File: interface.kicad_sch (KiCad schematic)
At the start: 58 parts

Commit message: More changes from review
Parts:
- removed C? (x3): C_100n_0402, antmicro-footprints:0402-cap, symbol antmicroCapacitors0402:C_100n_0402
- removed R? (x10): R_2k_0402, antmicro-footprints:0402-res, symbol antmicroResistors0402:R_2k_0402
- removed R? (x12): R_0R_0402, antmicro-footprints:0402-res, symbol antmicroResistors0402:R_0R_0402
- removed R? (x2): R_2k2_0402, antmicro-footprints:0402-res, symbol antmicroResistors0402:R_2k2_0402
- removed R?: R_10k_0402, antmicro-footprints:0402-res, symbol antmicroResistors0402:R_10k_0402
- removed SP? (x4): 9774110360, antmicro-footprints:Mounting_Wuerth_WA-SMSI-M3_H11mm_9774110360, symbol antmicroMechanicalParts:9774110360
- removed TP? (x10): TP, antmicro-footprints:TP-R-1.5, symbol antmicroTestPoints:TP
- removed U?: NTS0102DP, antmicro-footprints:TSSOP-8_W3mm, symbol antmicroLogicTranslatorsLevelShifters:NTS0102DP
- removed U?: PCA9547BS,118, antmicro-footprints:HVQFN24, symbol antmicroLogicSignalSwitchesMultiplexersDecoders:PCA9547BS,118
- added C? (x4): C_1u_0603, antmicro-footprints:0603-cap, symbol antmicroCapacitors0603:C_1u_0603
- added D? (x4): LTST-C190GKT, antmicro-footprints:LED_0603, symbol antmicroLEDIndicationDiscrete:LTST-C190GKT
- added F? (x4): 04671.25NR, antmicro-footprints:0603-Fuse-Littelfuse-0467, symbol antmicroFuses:04671.25NR
- added J?: WE_68715014522_ONE-SIDE, antmicro-footprints:WE_68715014522_ONE-SIDE, symbol antmicroFCCConnectors:WE_68715014522_ONE-SIDE
- added J?: WE_68715014022, antmicro-footprints:WE_68715014022, symbol antmicroFCCConnectors:WE_68715014022
- added R? (x2): R_470R_0402, antmicro-footprints:0402-res, symbol antmicroResistors0402:R_470R_0402
- added R? (x2): R_200R_0402, antmicro-footprints:0402-res, symbol antmicroResistors0402:R_200R_0402
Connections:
- net +3V3: now also F?.2, F?.2
- net CAM0_SCL: now also J?.40 (Pin_40)
- net CAM0_SDA: now also J?.39 (Pin_39)
- net CAM1_SCL: now also J?.42 (Pin_42)
- net CAM1_SDA: now also J?.41 (Pin_41)
- net CAM2_SCL: now also J?.42 (Pin_42)
- net CAM2_SDA: now also J?.41 (Pin_41)
- net CAM3_SCL: now also J?.40 (Pin_40)
- net CAM3_SDA: now also J?.39 (Pin_39)
- net CSI0_CLK_N: now also J?.28 (Pin_28)
- net CSI0_CLK_P: now also J?.29 (Pin_29)
- net CSI0_D0_N: now also J?.25 (Pin_25)
- net CSI0_D0_P: now also J?.26 (Pin_26)
- net CSI0_D1_N: now also J?.23 (Pin_23)
- net CSI0_D1_P: now also J?.24 (Pin_24)
- net CSI1_D0_N: now also J?.21 (Pin_21)
- net CSI1_D0_P: now also J?.22 (Pin_22)
- net CSI1_D1_N: now also J?.19 (Pin_19)
- net CSI1_D1_P: now also J?.20 (Pin_20)
- net CSI2_CLK_N: now also J?.10 (Pin_10)
- net CSI2_CLK_P: now also J?.11 (Pin_11)
- net CSI2_D0_N: now also J?.7 (Pin_7)
- net CSI2_D0_P: now also J?.8 (Pin_8)
- net CSI2_D1_N: now also J?.5 (Pin_5)
- net CSI2_D1_P: now also J?.6 (Pin_6)
- net CSI3_D0_N: now also J?.3 (Pin_3)
- net CSI3_D0_P: now also J?.4 (Pin_4)
- net CSI3_D1_N: now also J?.1 (Pin_1)
- net CSI3_D1_P: now also J?.2 (Pin_2)
- net CSI4_CLK_N: now also J?.29 (Pin_29)
- net CSI4_CLK_P: now also J?.28 (Pin_28)
- net CSI4_D0_N: now also J?.25 (Pin_25)
- net CSI4_D0_P: now also J?.26 (Pin_26)
- net CSI4_D1_N: now also J?.23 (Pin_23)
- net CSI4_D1_P: now also J?.24 (Pin_24)
- net CSI5_D0_N: now also J?.21 (Pin_21)
- net CSI5_D0_P: now also J?.22 (Pin_22)
- net CSI5_D1_N: now also J?.19 (Pin_19)
- net CSI5_D1_P: now also J?.20 (Pin_20)
- net CSI6_CLK_N: now also J?.10 (Pin_10)
- net CSI6_CLK_P: now also J?.11 (Pin_11)
- net CSI6_D0_N: now also J?.7 (Pin_7)
- net CSI6_D0_P: now also J?.8 (Pin_8)
- net CSI6_D1_N: now also J?.5 (Pin_5)
- net CSI6_D1_P: now also J?.6 (Pin_6)
- net CSI7_D0_N: now also J?.3 (Pin_3)
- net CSI7_D0_P: now also J?.4 (Pin_4)
- net CSI7_D1_N: now also J?.1 (Pin_1)
- net CSI7_D1_P: now also J?.2 (Pin_2)
- net GND: now also C?.2, C?.2, C?.2, C?.2, D?.2, D?.2, D?.2, D?.2, J?.12 (Pin_12), J?.12 (Pin_12), J?.15 (Pin_15), J?.15 (Pin_15), J?.18 (Pin_18), J?.18 (Pin_18), J?.27 (Pin_27), J?.27 (Pin_27), J?.30 (Pin_30), J?.30 (Pin_30), J?.9 (Pin_9), J?.9 (Pin_9)
- new net: C?.1, F?.1, J?.47 (Pin_47), J?.48 (Pin_48), R?.1 (x2)
- new net: C?.1, F?.1, J?.49 (Pin_49), J?.50 (Pin_50), R?.1 (x2)
- new net: D?.1, R?.2 (x4)
- new net +5V: F?.2, F?.2
- new net CAM1_RST_3V3: J?.33 (Pin_33)
- new net CAM_RST_3V3: J?.33 (Pin_33)
- new net VSYNC_CAM0_3V3: J?.32 (Pin_32)
- new net VSYNC_CAM1_3V3: J?.34 (Pin_34)
- new net VSYNC_CAM2_3V3: J?.34 (Pin_34)
- new net VSYNC_CAM3_3V3: J?.32 (Pin_32)
- no-connect marks 29 -> 51
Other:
- note added: "Bottom CSI"
- note added: "CAM 0"
- note added: "CAM 1"
- note added: "CAM 2"
- note added: "CAM 3"
- note added: "CAM3"
- note added: "Camera module interfaces"
- note added: "Control interface"
- note added: "Side CSI"
- note removed: "0b1110000R"
- note removed: "0x70h"
- note removed: "I2C Level Shifting"
- note removed: "I2C Multiplexer"
- note removed: "I2C address:"
- note removed: "To camera I2C interfaces"
- note removed: "Xavier mounting standoffs"

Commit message: Add TVS to wire connectors
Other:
- title: (none) -> Antmicro Jetson AGX CSI Adapter
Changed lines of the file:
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@@
   (paper "A3")
   (title_block
+    (title "Antmicro Jetson AGX CSI Adapter")
     (date "2022-07-20")
     (rev "1.0.0")

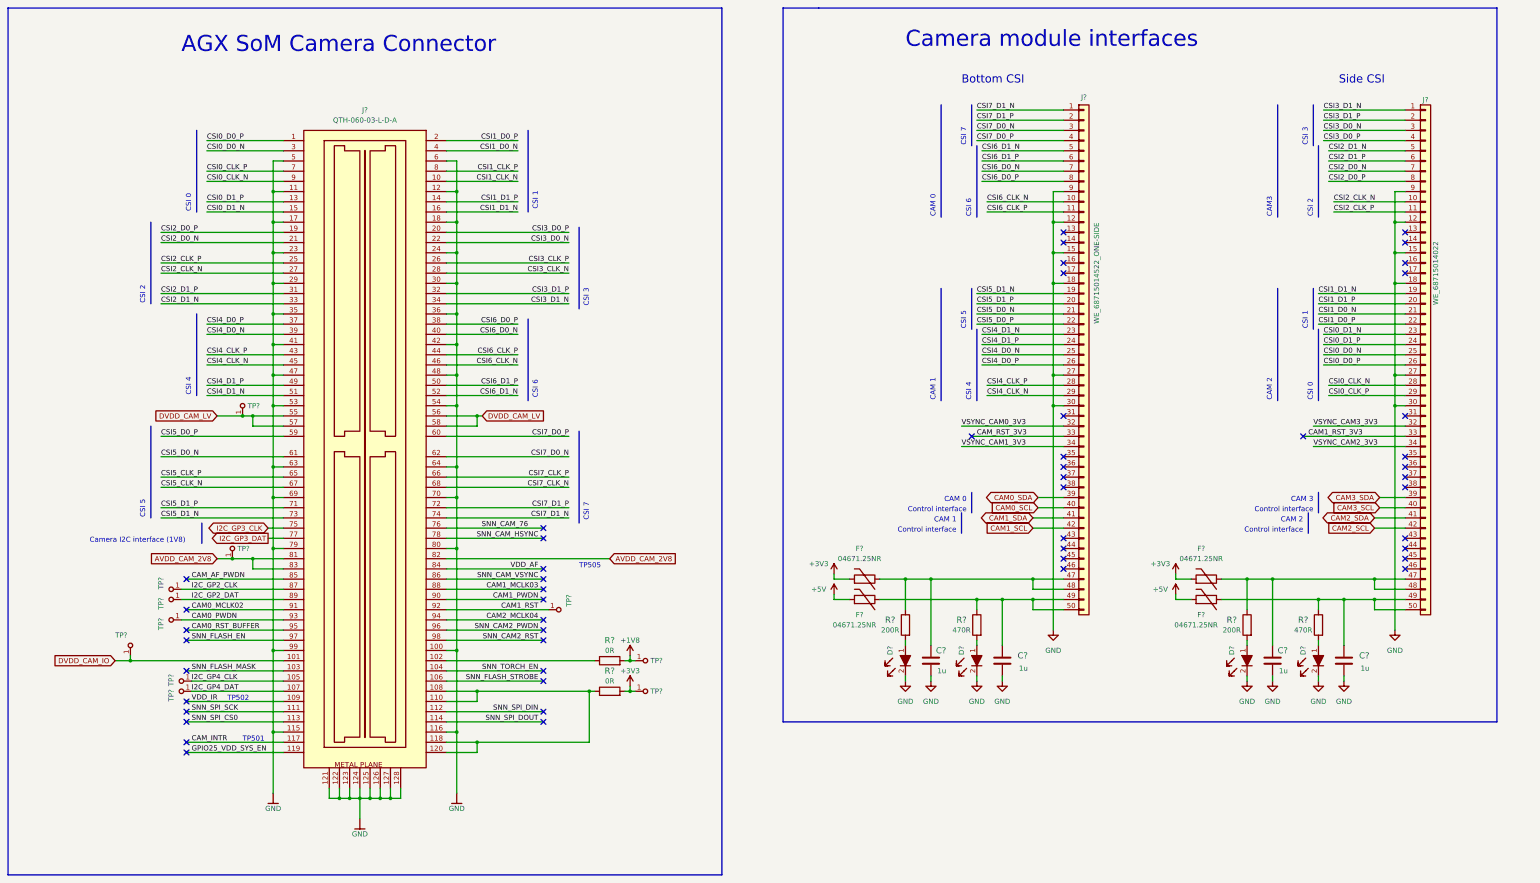
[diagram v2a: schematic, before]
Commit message: Routed CSI interface
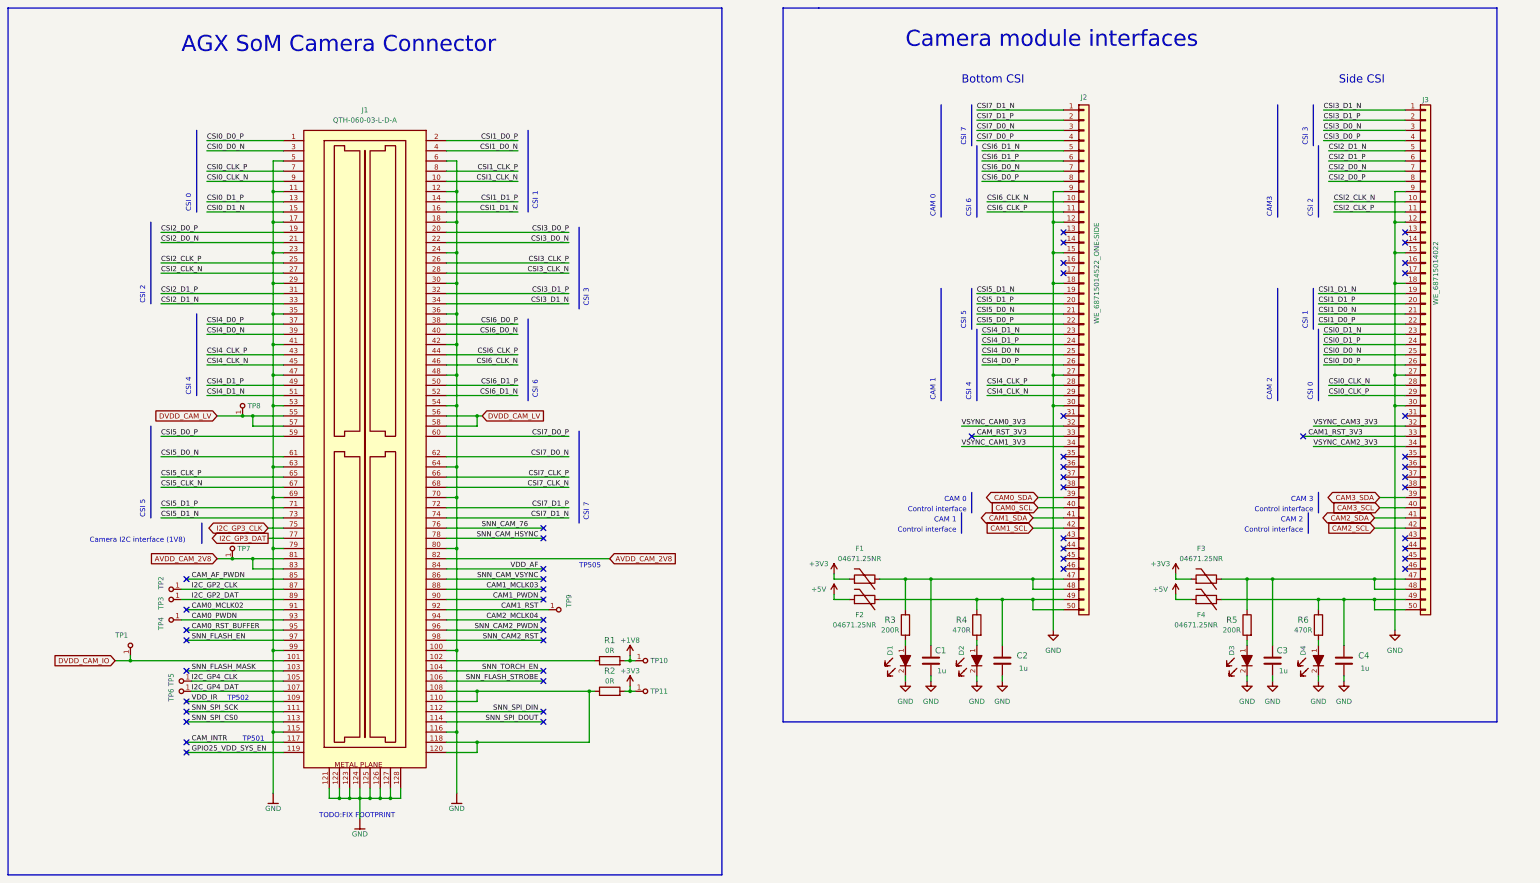
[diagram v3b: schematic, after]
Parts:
- gave numbers to parts that had none: 32
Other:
- note added: "TODO:FIX FOOTPRINT"

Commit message: Routed I2C signals, completed a layout of the voltage converter and I2C IC.
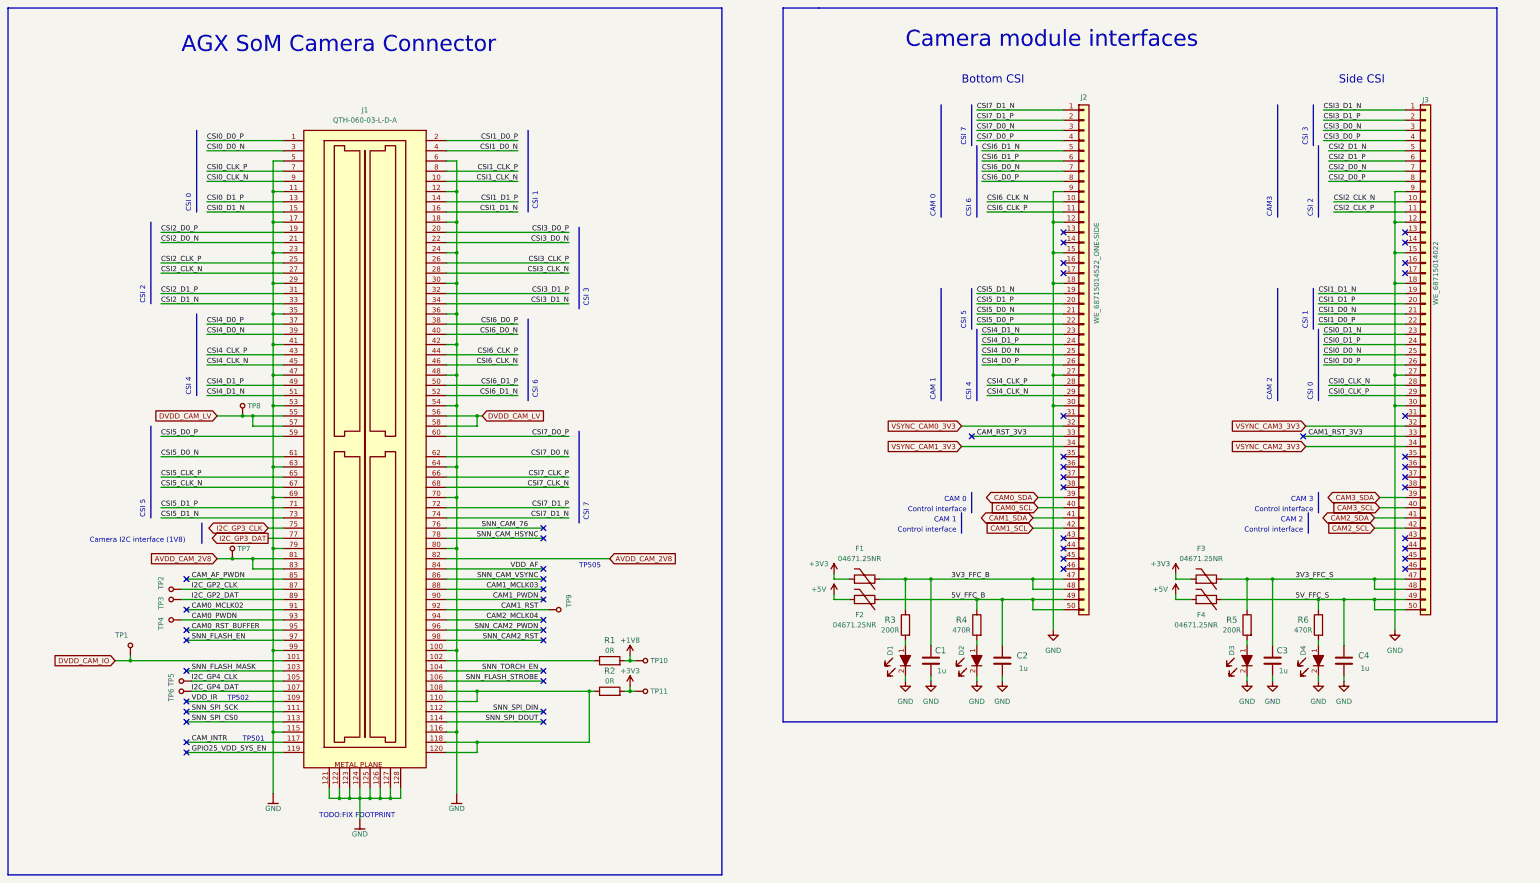
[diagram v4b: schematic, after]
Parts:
- TP1, TP10, TP11, TP2, TP3, TP4, TP5, TP6, TP7, TP8, TP9: value TP -> TP_SMD_0_75MM; footprint antmicro-footprints:TP-R-1.5 -> antmicro-footprints:Testpoint_smd_0_75mm; symbol antmicroTestPoints:TP -> antmicroTestPoints:TP_SMD_0_75MM
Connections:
- net 3V3_FFC_B: now reaches C1.1, F1.1, J2.47 (Pin_47), J2.48 (Pin_48), R3.1
- net 5V_FFC_B: now reaches C2.1, F2.1, J2.49 (Pin_49), J2.50 (Pin_50), R4.1
- net 5V_FFC_S: now reaches C4.1, F4.1, J3.49 (Pin_49), J3.50 (Pin_50), R6.1
- net 3V3_FFC_S: now reaches C3.1, F3.1, J3.47 (Pin_47), J3.48 (Pin_48), R5.1

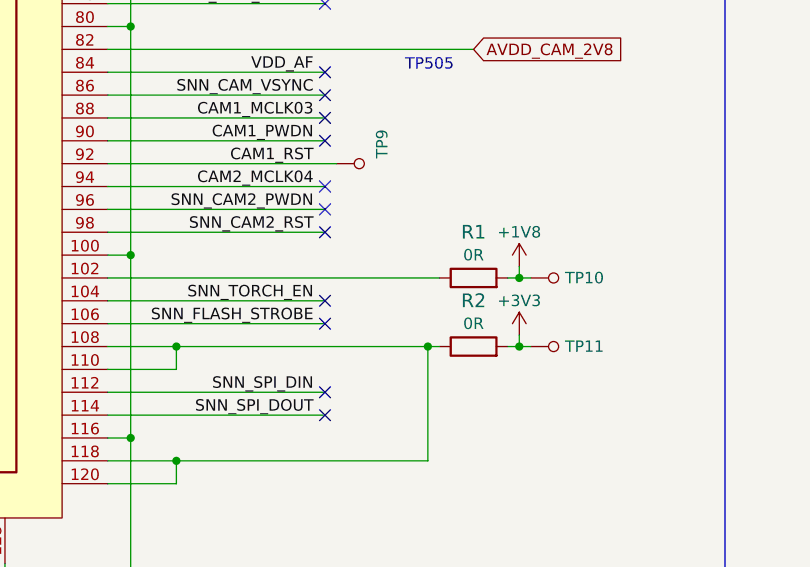
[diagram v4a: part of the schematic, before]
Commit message: Replaced some components with larger package, routed more signals
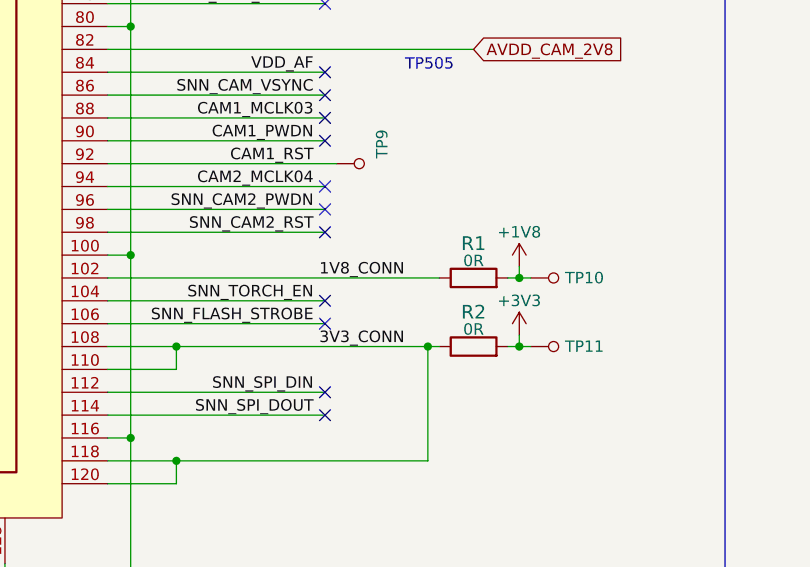
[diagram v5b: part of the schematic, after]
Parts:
- removed R1, R2: R_0R_0402, antmicro-footprints:0402-res, symbol antmicroResistors0402:R_0R_0402
- added R1, R2: R_0R_0805, antmicro-footprints:0805-res, symbol antmicroResistorsmisc:R_0R_0805
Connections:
- net +1V8: now also R1.2
- net +3V3: now also R2.2
- net 3V3_CONN: now reaches J1.108, J1.110, J1.118, J1.120
- net 3V3_CONN: now also R2.1
- net 1V8_CONN: now reaches J1.102
- net 1V8_CONN: now also R1.1
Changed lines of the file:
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@@
+    (effects (font (size 1.27 1.27)) (justify left bottom))
+  )
+  (label "1V8_CONN" (at 158.115 187.96 0)
     (effects (font (size 1.27 1.27)) (justify left bottom))
   )
@@
   )
   (label "CSI6_CLK_P" (at 269.24 76.2 0)
+    (effects (font (size 1.27 1.27)) (justify left bottom))
+  )
+  (label "3V3_CONN" (at 158.115 195.58 0)
     (effects (font (size 1.27 1.27)) (justify left bottom))
   )
@@
     (pin "8")
     (pin "9")
-  )
-  (symbol (lib_id "antmicroResistors0402:R_0R_0402") (at 175.26 195.58 0) (unit 1)
-    (in_bom yes) (on_board yes)
-    (property "Reference" "R2" (id 0) (at 175.26 190.5 0)
-      (effects (font (size 1.524 1.524)))
-    )
-    (property "Value" "R_0R_0402" (id 1) (at 175.26 199.39 0)
-      (effects (font (size 1.524 1.524)) hide)
-    )
-    (property "Footprint" "antmicro-footprints:0402-res" (id 2) (at 180.34 190.5 0)
-      (effects (font (size 1.524 1.524)) (justify left) hide)
-    )
-    (property "Datasheet" "" (id 3) (at 175.26 195.58 0)
-      (effects (font (size 1.27 1.27)) hide)
-    )
-    (property "Manufacturer" "PANASONIC" (id 4) (at 180.34 185.42 0)
-      (effects (font (size 1.524 1.524)) (justify left) hide)
-    )
-    (property "MPN" "ERJ2GE0R00X" (id 5) (at 180.34 187.96 0)
-      (effects (font (size 1.524 1.524)) (justify left) hide)
-    )
-    (property "Val" "0R" (id 6) (at 175.26 193.04 0))
-    (pin "1")
-    (pin "2")
   )
   (symbol (lib_id "antmicroLEDIndicationDiscrete:LTST-C190GKT") (at 248.92 189.23 90) (mirror x) (unit 1)
@@
     (pin "99")
   )
+  (symbol (lib_id "antmicroResistorsmisc:R_0R_0805") (at 175.26 187.96 0) (unit 1)
+    (in_bom yes) (on_board yes)
+    (property "Reference" "R1" (id 0) (at 175.26 184.15 0)
+      (effects (font (size 1.524 1.524)))
+    )
+    (property "Value" "R_0R_0805" (id 1) (at 175.26 191.77 0)
+      (effects (font (size 1.524 1.524)) hide)
+    )
+    (property "Footprint" "antmicro-footprints:0805-res" (id 2) (at 180.34 182.88 0)
+      (effects (font (size 1.524 1.524)) (justify left) hide)
+    )
+    (property "Datasheet" "" (id 3) (at 175.26 187.96 0)
+      (effects (font (size 1.27 1.27)) hide)
+    )
+    (property "Manufacturer" "VISHAY" (id 4) (at 180.34 177.8 0)
+      (effects (font (size 1.524 1.524)) (justify left) hide)
+    )
+    (property "MPN" "CRCW08050000Z0EA" (id 5) (at 180.34 180.34 0)
+      (effects (font (size 1.524 1.524)) (justify left) hide)
+    )
+    (property "Val" "0R" (id 6) (at 175.26 186.055 0))
+    (pin "1")
+    (pin "2")
+  )
   (symbol (lib_id "antmicroResistors0402:R_200R_0402") (at 248.92 179.07 90) (mirror x) (unit 1)
     (in_bom yes) (on_board yes)
@@
     (pin "1")
   )
-  (symbol (lib_id "antmicroResistors0402:R_0R_0402") (at 175.26 187.96 0) (unit 1)
-    (in_bom yes) (on_board yes)
-    (property "Reference" "R1" (id 0) (at 175.26 182.88 0)
+  (symbol (lib_id "antmicroResistorsmisc:R_0R_0805") (at 175.26 195.58 0) (unit 1)
+    (in_bom yes) (on_board yes)
+    (property "Reference" "R2" (id 0) (at 175.26 191.77 0)
       (effects (font (size 1.524 1.524)))
     )
-    (property "Value" "R_0R_0402" (id 1) (at 175.26 191.77 0)
+    (property "Value" "R_0R_0805" (id 1) (at 175.26 199.39 0)
       (effects (font (size 1.524 1.524)) hide)
     )
-    (property "Footprint" "antmicro-footprints:0402-res" (id 2) (at 180.34 182.88 0)
-      (effects (font (size 1.524 1.524)) (justify left) hide)
-    )
-    (property "Datasheet" "" (id 3) (at 175.26 187.96 0)
-      (effects (font (size 1.27 1.27)) hide)
-    )
-    (property "Manufacturer" "PANASONIC" (id 4) (at 180.34 177.8 0)
-      (effects (font (size 1.524 1.524)) (justify left) hide)
-    )
-    (property "MPN" "ERJ2GE0R00X" (id 5) (at 180.34 180.34 0)
-      (effects (font (size 1.524 1.524)) (justify left) hide)
-    )
-    (property "Val" "0R" (id 6) (at 175.26 185.42 0))
-    (pin "1")
-    (pin "2")
+    (property "Footprint" "antmicro-footprints:0805-res" (id 2) (at 180.34 190.5 0)
+      (effects (font (size 1.524 1.524)) (justify left) hide)
+    )
+    (property "Datasheet" "" (id 3) (at 175.26 195.58 0)
+      (effects (font (size 1.27 1.27)) hide)
+    )
+    (property "Manufacturer" "VISHAY" (id 4) (at 180.34 185.42 0)
+      (effects (font (size 1.524 1.524)) (justify left) hide)
+    )
+    (property "MPN" "CRCW08050000Z0EA" (id 5) (at 180.34 187.96 0)
+      (effects (font (size 1.524 1.524)) (justify left) hide)
+    )
+    (property "Val" "0R" (id 6) (at 175.26 193.675 0))
+    (pin "1")
+    (pin "2")
